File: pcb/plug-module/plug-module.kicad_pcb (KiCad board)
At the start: 2 copper layers, 70 x 100 mm, 15 parts, among them J1 Conn_01x10_Pin, J2 Conn_01x04_Pin, J3 Conn_01x15_Socket, J4 Conn_01x04_Pin, J5 Conn_01x10_Pin, Q1 BS170, U1 74HC688, U2 74AHC1G08, U3 74HC595

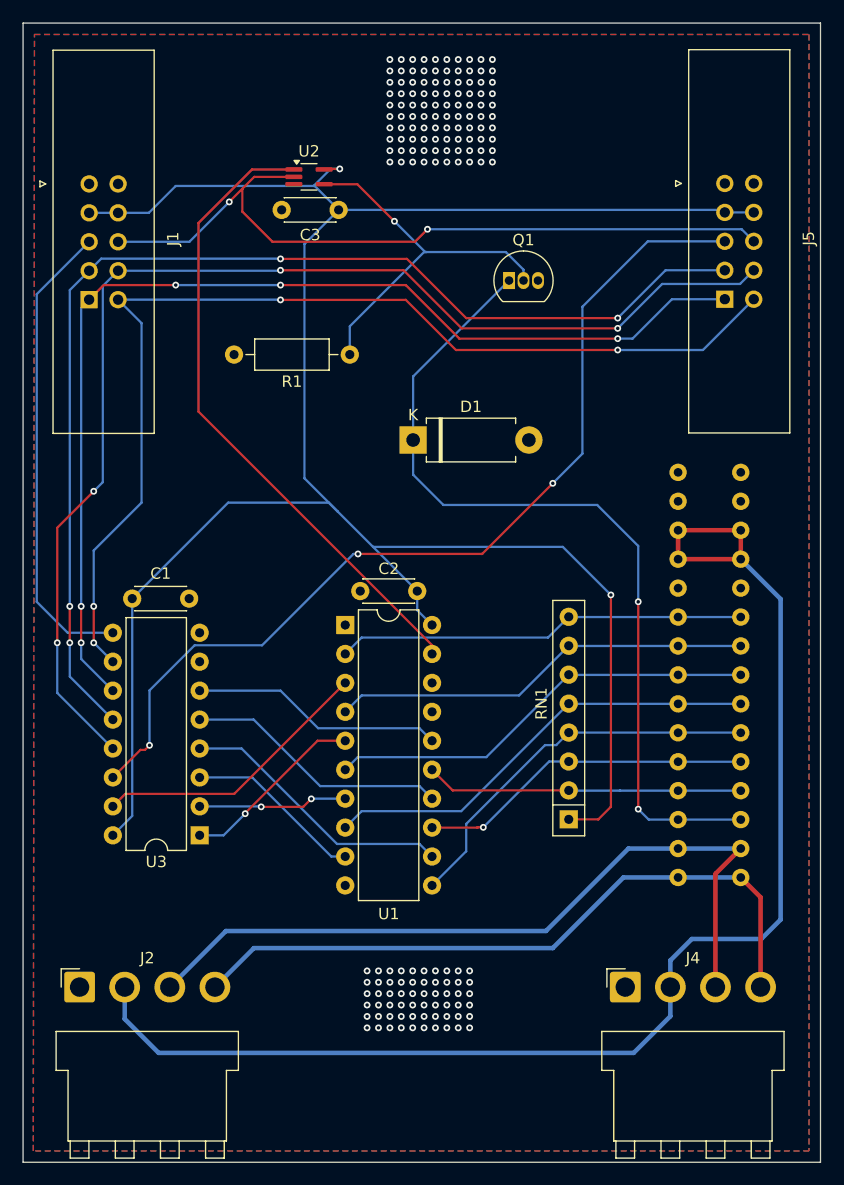
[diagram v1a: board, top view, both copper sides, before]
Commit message: plug module improvements (soldering)
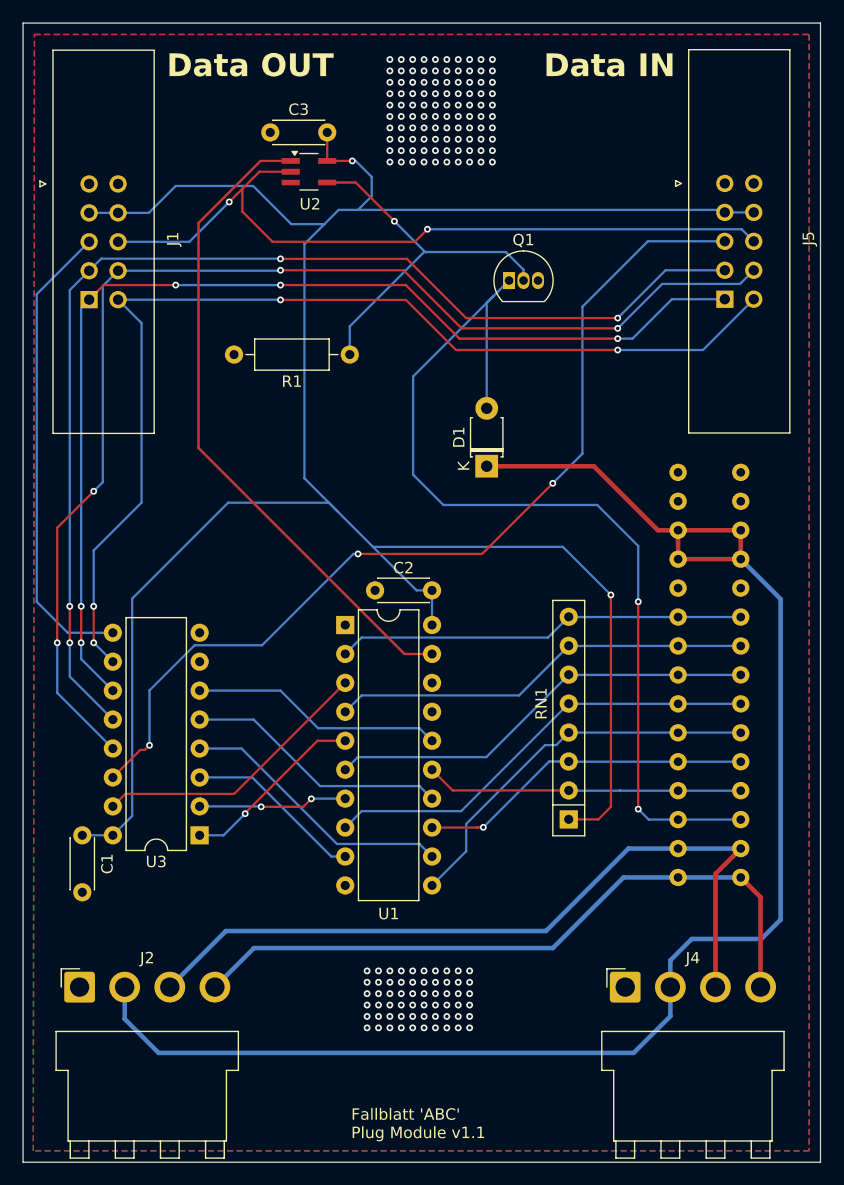
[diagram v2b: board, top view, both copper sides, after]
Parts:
- D1: value D -> 1N4148; footprint Diode_THT:D_DO-15_P10.16mm_Horizontal -> Diode_THT:D_T-1_P5.08mm_Horizontal
- U2: footprint Package_TO_SOT_SMD:SOT-353_SC-70-5_Handsoldering -> JS_Local:TSSOP-5_Handsoldering
- moved C1 21.2 mm to (135.2, 91.3), turned to -90 degrees
- moved C3 6.87 mm to (156.7, 29.6)
- moved D1 6.86 mm to (170.7, 58.9), turned to 90 degrees
- moved C2 1.30 mm to (165.9, 69.8)
- moved U2 0.45 mm to (155.1, 33.0)
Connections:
- net +5V renamed VCC
- D1 pad 1: /RELAIS_GND -> +24V
- D1 pad 2: GND -> /RELAIS_GND
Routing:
- net +24V: track 118.5 -> 137.6 mm
- net /RELAIS_GND: track 75.4 -> 85.4 mm
- net VCC: track 195.6 -> 204.4 mm
- net /NEQ: track 56.6 -> 58.1 mm
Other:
- board text added: "Data IN"
- board text added: "Data OUT"
- board text added: "Fallblatt 'ABC' Plug Module v1.1"

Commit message: first version firmware, rounded corners
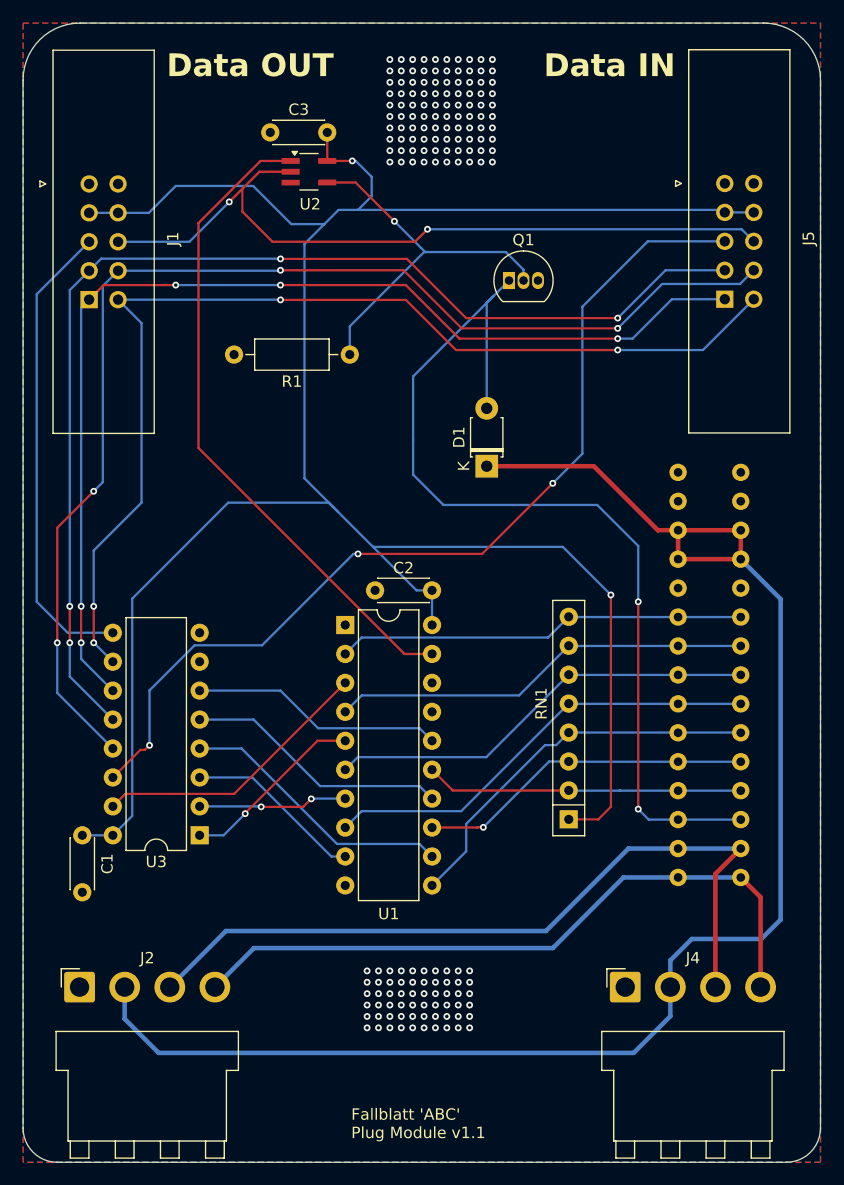
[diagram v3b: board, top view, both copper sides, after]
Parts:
- RN1: value 4K7 -> 100K
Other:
- outline, holes or cut-outs redrawn
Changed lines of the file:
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@@
 			)
 		)
-		(property "Value" "4K7"
+		(property "Value" "100K"
 			(at 10.16 2.4 90)
 			(layer "F.Fab")
@@
 		)
 	)
-	(gr_rect
-		(start 130 20)
-		(end 200 120)
+	(gr_arc
+		(start 133 120)
+		(mid 130.87868 119.12132)
+		(end 130 117)
+		(stroke
+			(width 0.05)
+			(type default)
+		)
+		(layer "Edge.Cuts")
+	)
+	(gr_line
+		(start 200 25)
+		(end 200 117)
+		(stroke
+			(width 0.05)
+			(type default)
+		)
+		(layer "Edge.Cuts")
+	)
+	(gr_arc
+		(start 130 25)
+		(mid 131.464466 21.464466)
+		(end 135 20)
+		(stroke
+			(width 0.05)
+			(type default)
+		)
+		(layer "Edge.Cuts")
+	)
+	(gr_arc
+		(start 195 20)
+		(mid 198.535534 21.464466)
+		(end 200 25)
+		(stroke
+			(width 0.05)
+			(type default)
+		)
+		(layer "Edge.Cuts")
+	)
+	(gr_line
+		(start 135 20)
+		(end 195 20)
+		(stroke
+			(width 0.05)
+			(type default)
+		)
+		(layer "Edge.Cuts")
+	)
+	(gr_line
+		(start 197 120)
+		(end 133 120)
+		(stroke
+			(width 0.05)
+			(type default)
+		)
+		(layer "Edge.Cuts")
+	)
+	(gr_arc
+		(start 200 117)
+		(mid 199.12132 119.12132)
+		(end 197 120)
+		(stroke
+			(width 0.05)
+			(type default)
+		)
+		(layer "Edge.Cuts")
+	)
+	(gr_line
+		(start 130 117)
+		(end 130 25)
 		(stroke
 			(width 0.05)
 			(type default)
 		)
-		(fill none)
 		(layer "Edge.Cuts")
 	)
@@
 		(polygon
 			(pts
-				(xy 131 21) (xy 199 21) (xy 199 119) (xy 130.9 119)
+				(xy 130 20) (xy 200 20) (xy 200 120) (xy 130 120)
 			)
 		)
@@
 		(polygon
 			(pts
-				(xy 131 21) (xy 199 21) (xy 199 119) (xy 130.9 119)
+				(xy 130 20) (xy 200 20) (xy 200 120) (xy 130 120)
 			)
 		)

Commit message: pcb layout plug module
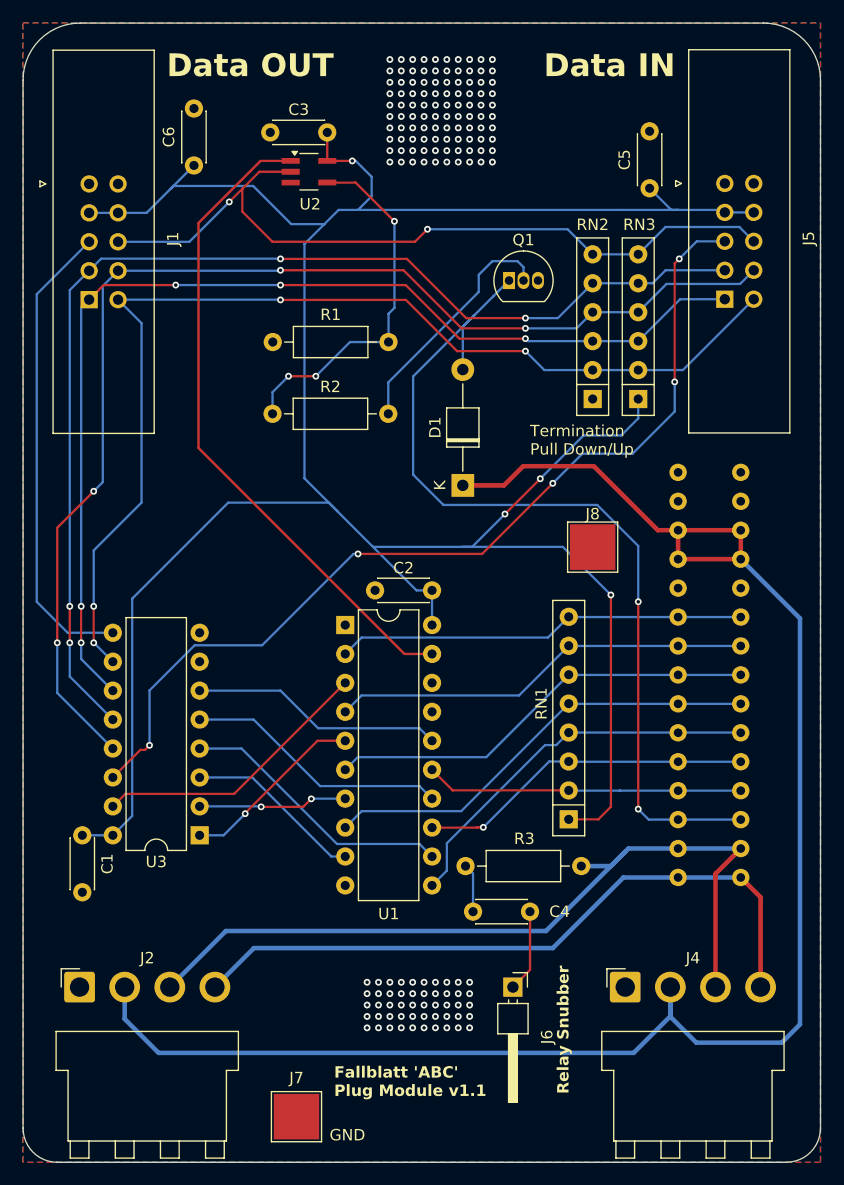
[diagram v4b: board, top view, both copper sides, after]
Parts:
- added C4: 2u2, Capacitor_THT:C_Disc_D4.3mm_W1.9mm_P5.00mm, F.Cu at (169.5, 98.0)
- added C5: 100n, Capacitor_THT:C_Disc_D4.3mm_W1.9mm_P5.00mm, F.Cu at (185.0, 34.5)
- added C6: 100n, Capacitor_THT:C_Disc_D4.3mm_W1.9mm_P5.00mm, F.Cu at (145.0, 32.5)
- added J6: Conn_01x01_Pin, Connector_PinHeader_2.54mm:PinHeader_1x01_P2.54mm_Horizontal, F.Cu at (173.0, 104.6)
- added J7: Conn_01x01_Pin, TestPoint:TestPoint_Pad_4.0x4.0mm, F.Cu at (154.0, 116.0)
- added J8: Conn_01x01_Pin, TestPoint:TestPoint_Pad_4.0x4.0mm, F.Cu at (180.0, 66.0)
- added R2: 5K6, Resistor_THT:R_Axial_DIN0207_L6.3mm_D2.5mm_P10.16mm_Horizontal, F.Cu at (151.9, 54.3)
- added R3: 10, Resistor_THT:R_Axial_DIN0207_L6.3mm_D2.5mm_P10.16mm_Horizontal, F.Cu at (179.0, 94.0)
- added RN2: R_Network05, Resistor_THT:R_Array_SIP6, F.Cu at (180.0, 53.0)
- added RN3: R_Network05, Resistor_THT:R_Array_SIP6, F.Cu at (184.0, 53.0)
- D1: footprint Diode_THT:D_T-1_P5.08mm_Horizontal -> Diode_THT:D_T-1_P10.16mm_Horizontal
- moved R1 3.57 mm to (162.1, 48.0)
- moved D1 2.69 mm to (168.6, 60.6)
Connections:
- R1 pad 1: Net-(Q1-G) -> Net-(R1-Pad1)
- U2 pad 4: Net-(Q1-G) -> Net-(R1-Pad1)
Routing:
- net Net-(R1-Pad1): track 0.00 -> 32.0 mm, vias 0 -> 3
- net VCC: track 204.4 -> 232.5 mm, vias 2 -> 4
- net +24V: track 137.6 -> 152.4 mm
- net Net-(Q1-G): track 33.2 -> 21.3 mm, vias 1 -> 0
- net Net-(J6-Pin_1): track 0.00 -> 7.25 mm
- net /RELAIS_GND: track 85.4 -> 80.6 mm
- net /24VAC_N: track 68.2 -> 72.7 mm
- net Net-(C4-Pad1): track 0.00 -> 4.27 mm
- net /SPIN_ENABLE: track 66.6 -> 68.6 mm
- net /SHIFT_CLEAR: track 94.6 -> 96.0 mm
- net /DATA_IN: track 83.6 -> 83.7 mm, vias 3 -> 5
- net GND: vias 160 -> 150
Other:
- board text added: "GND"
- board text added: "Relay Snubber"
- board text added: "Termination Pull Down/Up"

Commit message: many improvements
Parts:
- added J10: Conn_01x01_Pin, JS_Local:Langloch-Pad, F.Cu at (150.1, 25.0)
- added J9: Conn_01x01_Pin, JS_Local:Langloch-Pad, F.Cu at (179.9, 25.0)
- moved J6 23.5 mm to (153.0, 117.0), turned to 90 degrees
- moved J7 22.7 mm to (176.7, 114.6)
- moved C6 1.51 mm to (143.5, 32.3)
- turned C3 to 0 degrees
- turned C5 to 180 degrees
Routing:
- net Net-(J6-Pin_1): track 7.25 -> 38.5 mm, vias 0 -> 1
- net VCC: track 232.5 -> 232.0 mm
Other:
- board text added: "Fallblatt Adtranz 'ABC' Plug Module v1.1"
- board text added: "Relay Snubber (connect to '?')"
- board text removed: "Fallblatt 'ABC' Plug Module v1.1"
- board text removed: "Relay Snubber"

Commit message: graytable, both pcbs
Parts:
- removed RN2, RN3: R_Network05, Resistor_THT:R_Array_SIP6
- added R10: R, Resistor_SMD:R_1206_3216Metric_Pad1.30x1.75mm_HandSolder, F.Cu at (183.8, 51.0)
- added R11: R, Resistor_SMD:R_1206_3216Metric_Pad1.30x1.75mm_HandSolder, F.Cu at (183.8, 41.1)
- added R12: R, Resistor_SMD:R_1206_3216Metric_Pad1.30x1.75mm_HandSolder, F.Cu at (183.8, 44.4)
- added R13: R, Resistor_SMD:R_1206_3216Metric_Pad1.30x1.75mm_HandSolder, F.Cu at (183.8, 37.8)
- added R4: R, Resistor_SMD:R_1206_3216Metric_Pad1.30x1.75mm_HandSolder, F.Cu at (178.3, 47.7)
- added R5: R, Resistor_SMD:R_1206_3216Metric_Pad1.30x1.75mm_HandSolder, F.Cu at (178.3, 51.0)
- added R6: R, Resistor_SMD:R_1206_3216Metric_Pad1.30x1.75mm_HandSolder, F.Cu at (178.3, 41.1)
- added R7: R, Resistor_SMD:R_1206_3216Metric_Pad1.30x1.75mm_HandSolder, F.Cu at (178.3, 44.4)
- added R8: R, Resistor_SMD:R_1206_3216Metric_Pad1.30x1.75mm_HandSolder, F.Cu at (178.3, 37.8)
- added R9: R, Resistor_SMD:R_1206_3216Metric_Pad1.30x1.75mm_HandSolder, F.Cu at (183.8, 47.7)
- J6: moved to B.Cu
- moved R1 10.3 mm to (151.9, 49.9), turned to 0 degrees
- moved Q1 6.61 mm to (168.5, 37.5)
- moved C3 3.83 mm to (159.6, 32.1), turned to 90 degrees
- moved U2 3.62 mm to (157.2, 36.0)
- turned C6 to 0 degrees
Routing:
- net VCC: track 232.0 -> 220.9 mm, vias 4 -> 5
- net Net-(R1-Pad1): track 32.0 -> 21.7 mm
- net /SPIN_ENABLE: track 68.6 -> 73.4 mm, vias 2 -> 4
- net /RELAIS_GND: track 80.6 -> 84.9 mm
- net /SHIFT_LATCH: track 101.8 -> 104.8 mm, vias 4 -> 5
- net /SHIFT_CLEAR: track 96.0 -> 98.9 mm, vias 4 -> 5
- net /SHIFT_CLOCK: track 95.7 -> 98.1 mm, vias 5 -> 6
- net /SHIFT_OUTPUT_ENABLE: track 106.2 -> 108.7 mm, vias 4 -> 5
- net Net-(Q1-G): track 21.3 -> 20.0 mm, vias 0 -> 2
- net /NEQ: track 58.1 -> 58.9 mm
- net /DATA_IN: track 83.7 -> 84.2 mm
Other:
- board text added: "DOWN"
- board text added: "Relay Snubber (connect to 'b')"
- board text added: "Termination"
- board text added: "UP"
- board text removed: "Relay Snubber (connect to '?')"
- board text removed: "Termination Pull Down/Up"

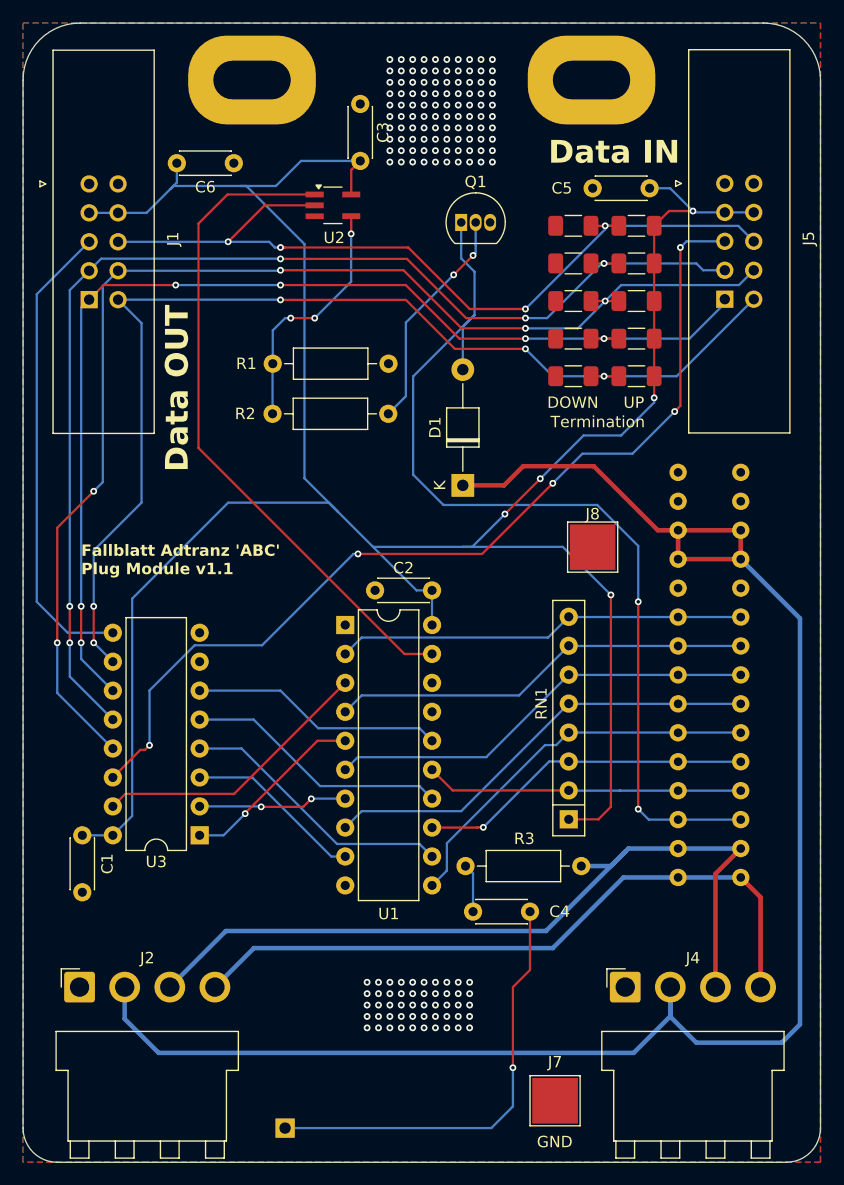
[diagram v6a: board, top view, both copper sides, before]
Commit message: plug module pp snubber
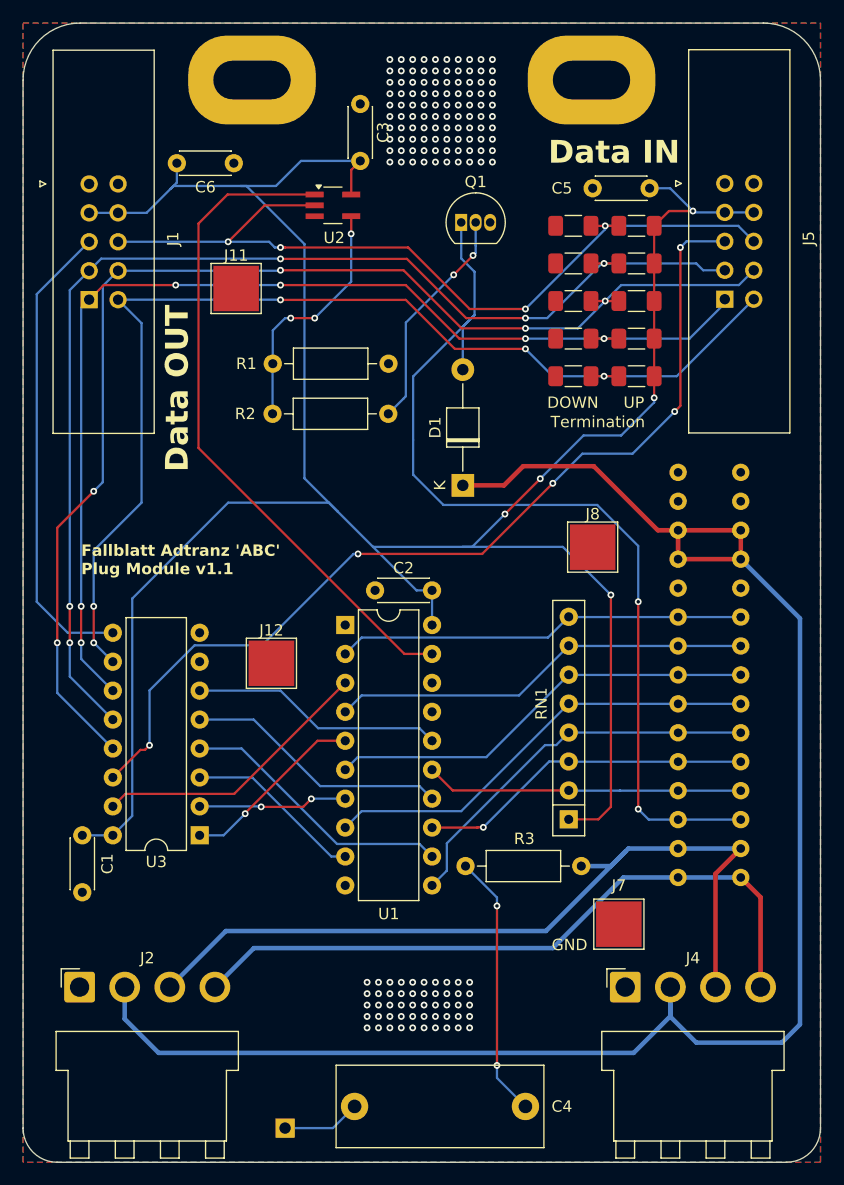
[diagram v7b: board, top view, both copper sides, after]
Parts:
- added J11: Conn_01x01_Pin, TestPoint:TestPoint_Pad_4.0x4.0mm, F.Cu at (148.7, 43.3)
- added J12: Conn_01x01_Pin, TestPoint:TestPoint_Pad_4.0x4.0mm, F.Cu at (151.8, 76.2)
- C4: footprint Capacitor_THT:C_Disc_D4.3mm_W1.9mm_P5.00mm -> Capacitor_THT:C_Rect_L18.0mm_W7.0mm_P15.00mm_FKS3_FKP3
- D1: value 1N4148 -> 1N4148/1N4003
- moved C4 17.7 mm to (174.1, 115.1), turned to 180 degrees
- moved J7 16.5 mm to (182.3, 99.1)
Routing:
- net Net-(J6-Pin_1): track 38.5 -> 6.89 mm, vias 1 -> 0
- net Net-(C4-Pad1): track 4.27 -> 23.3 mm, vias 0 -> 2

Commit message: labels, datasheet, circuit doku
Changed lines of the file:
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@@
 		(tags "C Rect series Radial pin pitch 15.00mm  length 18mm width 7mm Capacitor")
 		(property "Reference" "C4"
-			(at -3.2 0 360)
+			(at -3.2 0 0)
 			(layer "F.SilkS")
 			(effects
@@
 		)
 		(property "Value" "2u2"
-			(at 7.5 4.75 360)
+			(at 7.5 4.75 0)
 			(layer "F.Fab")
 			(effects
@@
 		)
 		(fp_text user "${REFERENCE}"
-			(at 7.5 0 360)
+			(at 7.5 0 0)
 			(layer "F.Fab")
 			(effects
@@
 		(tags "C Disc series Radial pin pitch 5.00mm  diameter 4.3mm width 1.9mm Capacitor")
 		(property "Reference" "C3"
-			(at 2.5 2 90)
+			(at 2.5 -2.5 180)
 			(layer "F.SilkS")
 			(effects
@@
 			(font
 				(size 1 1)
-				(thickness 0.1)
+				(thickness 0.15)
 			)
 			(justify left bottom)
@@
 		)
 	)
+	(gr_text "GND"
+		(at 171.1 22.6 0)
+		(layer "F.SilkS")
+		(effects
+			(font
+				(size 1 1)
+				(thickness 0.15)
+			)
+			(justify left bottom)
+		)
+	)
 	(gr_text "Fallblatt Adtranz 'ABC'\nPlug Module v1.1"
 		(at 135.1 68.5 0)
@@
 			)
 			(justify left bottom)
+		)
+	)
+	(gr_text "GND"
+		(at 155.8 22.6 0)
+		(layer "F.SilkS")
+		(effects
+			(font
+				(size 1 1)
+				(thickness 0.15)
+			)
+			(justify left bottom)
